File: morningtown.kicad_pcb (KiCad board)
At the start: 2 copper layers, 30 x 95 mm, 13 parts, among them SW1 Test, U1 Pico, U2 DS3231M

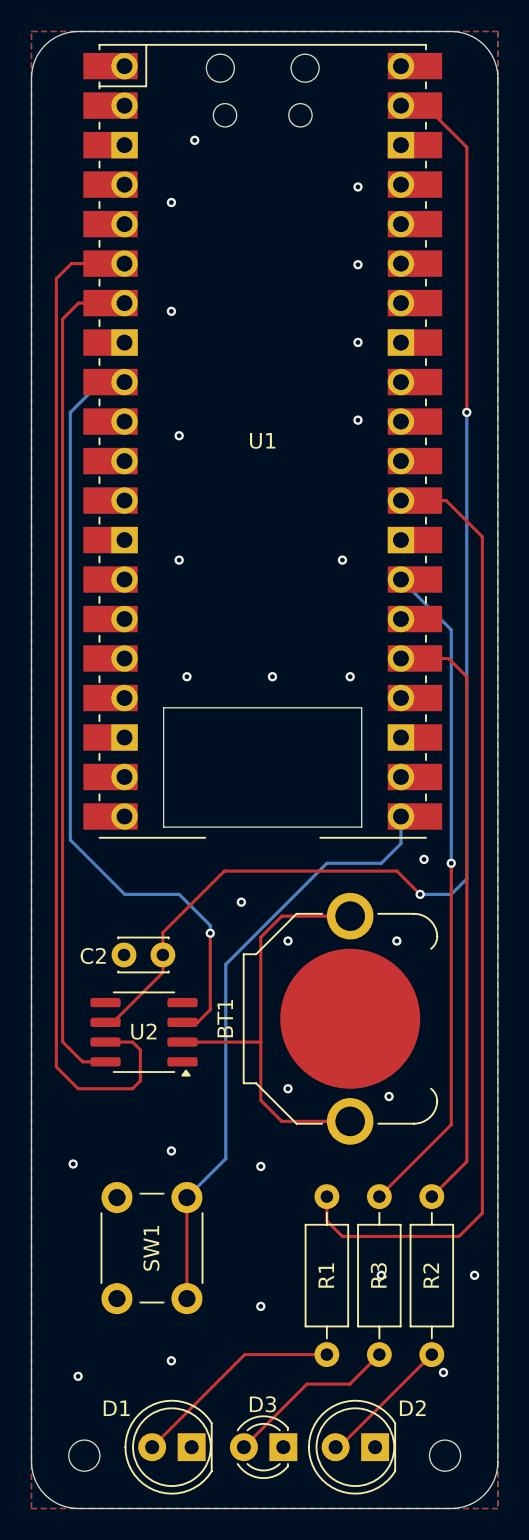
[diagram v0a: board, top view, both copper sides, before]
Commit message: Fix r1.0 errata
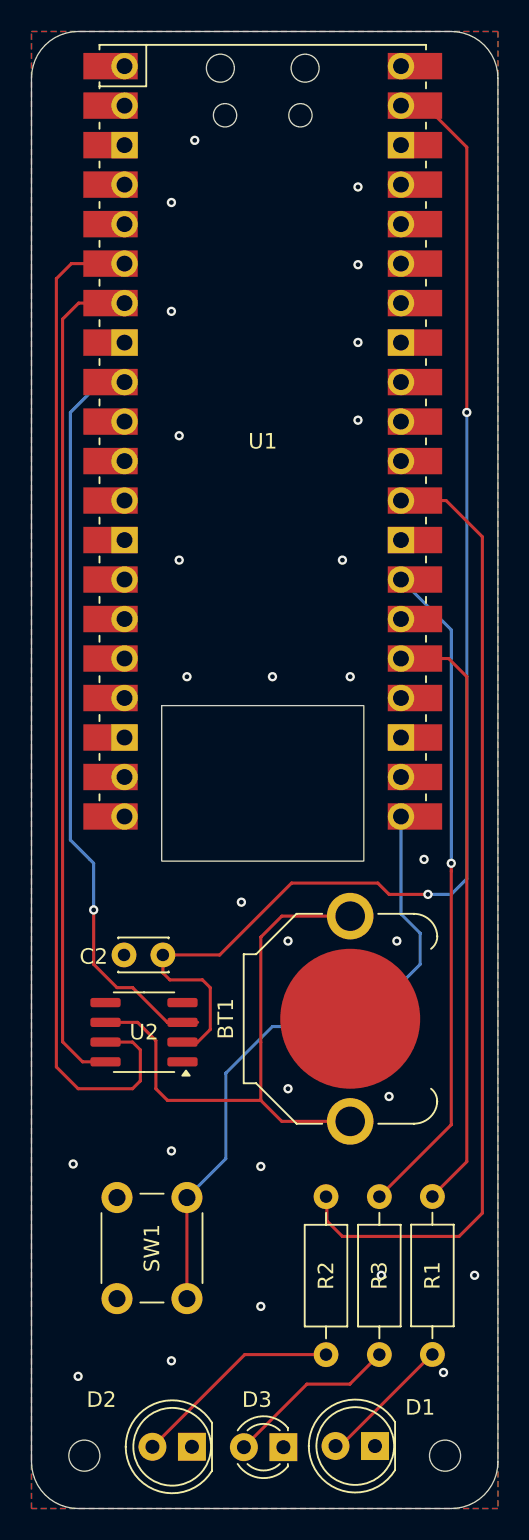
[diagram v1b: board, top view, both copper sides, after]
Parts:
- moved D1 11.8 mm to (142.1, 151.0)
- moved D2 11.8 mm to (130.3, 151.0)
- moved R2 6.81 mm to (138.9, 134.9)
- moved R1 6.79 mm to (145.8, 134.9)
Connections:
- R1 pad 1: Net-(U1-GPIO22) -> Net-(U1-GPIO19)
- R2 pad 1: Net-(U1-GPIO19) -> Net-(U1-GPIO22)
- U2 pad 2: Net-(BT1-+) -> Net-(U1-VSYS)
- U2 pad 6: Net-(U1-VSYS) -> Net-(BT1-+)
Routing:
- net Net-(BT1-+): track 28.2 -> 37.0 mm
- net Net-(D2-A): track 8.91 -> 13.7 mm
- net Net-(D1-A): track 13.7 -> 8.91 mm
- net Net-(U1-GPIO16): track 38.9 -> 41.1 mm
- net Net-(U1-GPIO6): track 50.6 -> 48.6 mm
- net Net-(U1-VSYS): track 82.2 -> 84.0 mm
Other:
- outline, holes or cut-outs redrawn
- board text added: "MorningTown rev 1.1"
- board text removed: "MorningTown rev 1.0"

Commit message: Switch to SMD resistors and capacitors
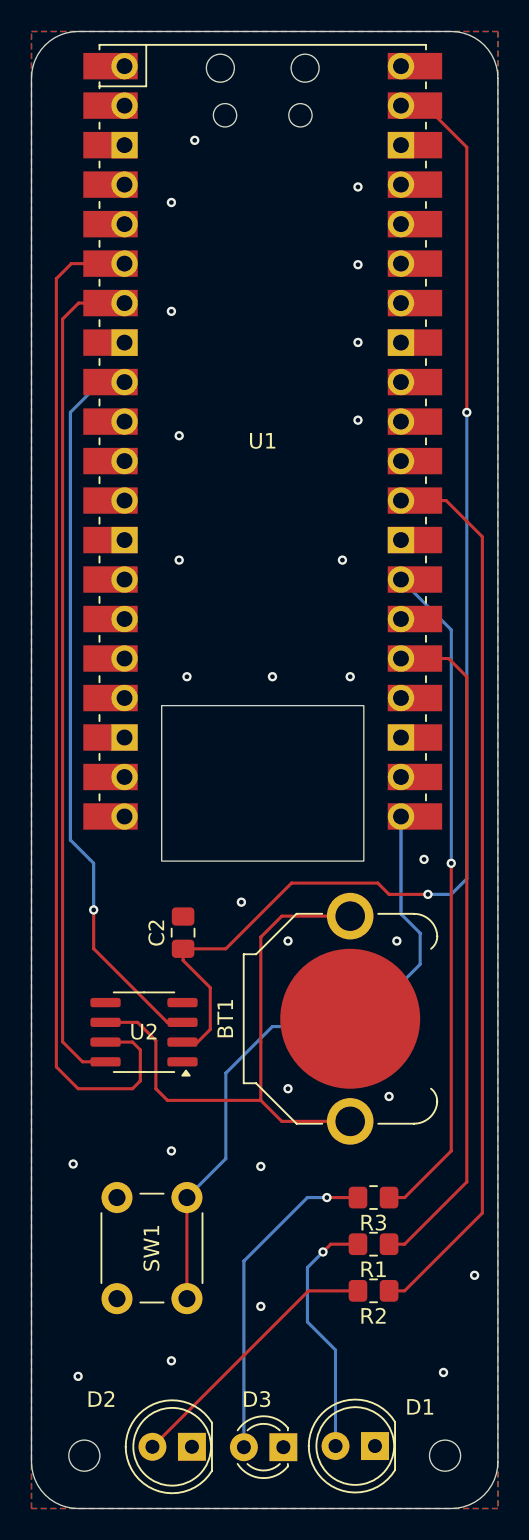
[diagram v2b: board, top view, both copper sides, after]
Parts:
- C2: value C_Small -> 1 µF; footprint Capacitor_THT:C_Disc_D3.0mm_W2.0mm_P2.50mm -> Capacitor_SMD:C_0805_2012Metric_Pad1.18x1.45mm_HandSolder
- R1, R2, R3: footprint Resistor_THT:R_Axial_DIN0207_L6.3mm_D2.5mm_P10.16mm_Horizontal -> Resistor_SMD:R_0805_2012Metric_Pad1.20x1.40mm_HandSolder
- moved R2 6.78 mm to (142.0, 141.0), turned to 180 degrees
- moved R1 4.87 mm to (142.0, 138.0), turned to 180 degrees
- moved C2 1.93 mm to (129.8, 118.0), turned to 90 degrees
- moved R3 0.38 mm to (142.0, 135.0), turned to 180 degrees
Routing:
- net Net-(D3-A): track 11.2 -> 21.0 mm, vias 0 -> 1
- net Net-(D1-A): track 8.91 -> 16.4 mm, vias 0 -> 1
- net Net-(U1-GPIO19): track 39.1 -> 43.9 mm
- net Net-(U1-GPIO22): track 62.3 -> 57.8 mm
- net Net-(D2-A): track 13.7 -> 17.4 mm
- net Net-(U1-VSYS): track 84.0 -> 81.1 mm
- net Net-(U1-GPIO6): track 48.6 -> 47.1 mm
- net GND: vias 28 -> 27
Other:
- board text added: "MorningTown rev 1.2"
- board text removed: "MorningTown rev 1.1"

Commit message: General tidy-up
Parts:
- moved R2 14.4 mm to (128.8, 146.7)
- moved R3 13.8 mm to (134.7, 146.7)
- moved R1 8.79 mm to (140.6, 146.7)
- moved C2 2.39 mm to (130.6, 120.2), turned to 180 degrees
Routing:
- net Net-(U1-GPIO21): track 43.3 -> 60.5 mm
- net Net-(D3-A): track 21.0 -> 4.39 mm, vias 1 -> 0
- net Net-(U1-GPIO22): track 57.8 -> 73.8 mm, vias 0 -> 2
- net Net-(D2-A): track 17.4 -> 4.37 mm
- net Net-(D1-A): track 16.4 -> 4.32 mm, vias 1 -> 0
- net Net-(U1-GPIO19): track 43.9 -> 53.1 mm
- net Net-(U1-GPIO16): track 41.1 -> 36.8 mm
- net Net-(U1-VSYS): track 81.1 -> 78.6 mm
- net Net-(U1-GPIO4): track 66.1 -> 64.0 mm
- net GND: vias 27 -> 28
